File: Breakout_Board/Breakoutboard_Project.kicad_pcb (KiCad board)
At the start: 2 copper layers, 1 part

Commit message: Added costum footprint
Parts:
- added U1: ADXL380-2BCCZ-RL7, ADXL380:CC-14-3_ADI, F.Cu at (97.8, 71.6)
- added U2: STM32F411CCUx, Package_DFN_QFN:QFN-48-1EP_7x7mm_P0.5mm_EP5.6x5.6mm, F.Cu at (100.5, 64.7)

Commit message: added the costum things to main pcb and sch
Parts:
- added U2: ~, SeniorDesignLibrary:BlackpillGeneric, F.Cu at (69.0, 78.1)

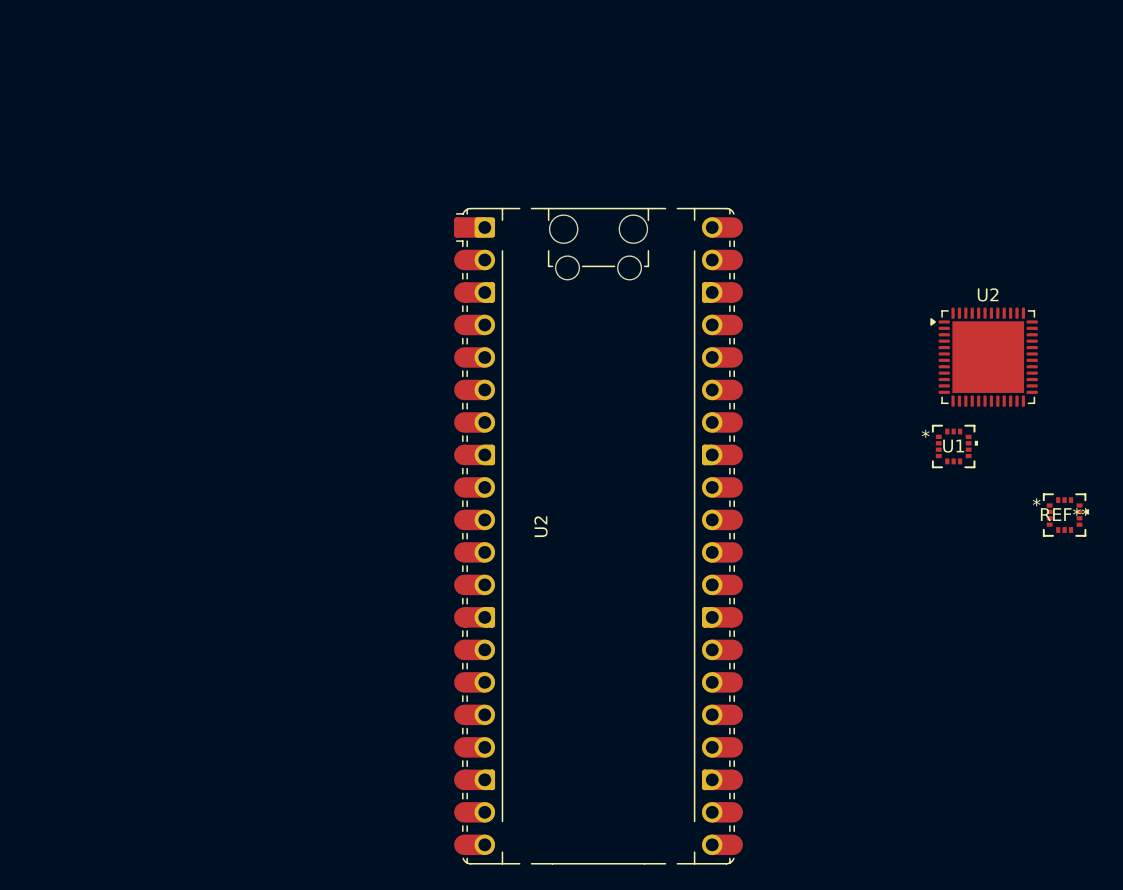
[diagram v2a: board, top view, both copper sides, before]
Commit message: added more organization
heriarchical sheets yay, added all the compoennts we will be working with and seperated into sheets so we can work on the in parralel easier.
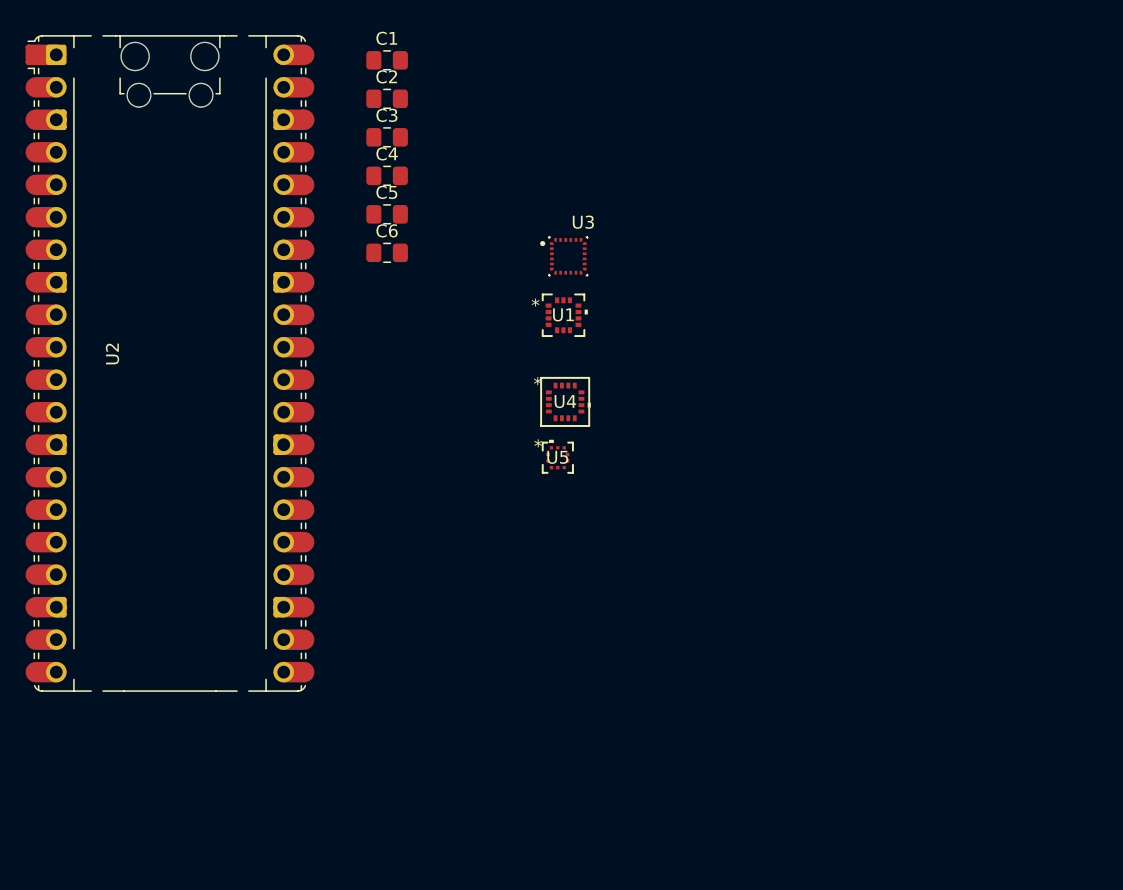
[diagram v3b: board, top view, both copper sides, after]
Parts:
- removed REF**: CC-14-3_ADI, ADXL380:CC-14-3_ADI
- removed the U2 at (69.0, 78.1)
- removed the U2 at (100.5, 64.7)
- added C1: .1uf, Capacitor_SMD:C_0805_2012Metric_Pad1.18x1.45mm_HandSolder, F.Cu at (53.5, 41.5)
- added C2: 1uf, Capacitor_SMD:C_0805_2012Metric_Pad1.18x1.45mm_HandSolder, F.Cu at (53.5, 44.5)
- added C3: 10uf, Capacitor_SMD:C_0805_2012Metric_Pad1.18x1.45mm_HandSolder, F.Cu at (53.5, 47.5)
- added C4: .1uf, Capacitor_SMD:C_0805_2012Metric_Pad1.18x1.45mm_HandSolder, F.Cu at (53.5, 50.5)
- added C5: 1uf, Capacitor_SMD:C_0805_2012Metric_Pad1.18x1.45mm_HandSolder, F.Cu at (53.5, 53.5)
- added C6: 10uf, Capacitor_SMD:C_0805_2012Metric_Pad1.18x1.45mm_HandSolder, F.Cu at (53.5, 56.5)
- added U2: STM32F411, SeniorDesignLibrary:BlackpillGeneric, F.Cu at (35.5, 64.6)
- added U3: ICM-40609-D, ICM-40609-D:XDCR_ICM-40609-D, F.Cu at (67.7, 56.8)
- added U4: MMC5983MA, MMC5983MA:MMC5983MA_MEM, F.Cu at (67.5, 68.2)
- added U5: BMP581, BMP581:QFN10_BMP581_BOS, F.Cu at (66.9, 72.5)
- moved U1 32.2 mm to (67.3, 61.4)

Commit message: changing around some things
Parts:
- added C11: .1uf, Capacitor_SMD:C_0805_2012Metric_Pad1.18x1.45mm_HandSolder, F.Cu at (115.0, 23.5)
- added C12: .1uf, Capacitor_SMD:C_0805_2012Metric_Pad1.18x1.45mm_HandSolder, F.Cu at (115.0, 26.5)
- added C13: .1uf, Capacitor_SMD:C_0805_2012Metric_Pad1.18x1.45mm_HandSolder, F.Cu at (115.0, 29.5)
- added C14: 1uf, Capacitor_SMD:C_0805_2012Metric_Pad1.18x1.45mm_HandSolder, F.Cu at (115.0, 32.5)
- added C15: 1uf, Capacitor_SMD:C_0805_2012Metric_Pad1.18x1.45mm_HandSolder, F.Cu at (115.0, 35.5)
- added C7: .1uf, Capacitor_SMD:C_0805_2012Metric_Pad1.18x1.45mm_HandSolder, F.Cu at (115.0, 14.4)
- added C8: 1uf, Capacitor_SMD:C_0805_2012Metric_Pad1.18x1.45mm_HandSolder, F.Cu at (115.0, 17.4)
- added C9: 10uf, Capacitor_SMD:C_0805_2012Metric_Pad1.18x1.45mm_HandSolder, F.Cu at (115.0, 20.4)
- added D1: ESD5Zxx, Diode_SMD:D_SOD-523, F.Cu at (124.8, 14.2)
- added D2: ESD5Zxx, Diode_SMD:D_SOD-523, F.Cu at (124.8, 16.6)
- added D3: ESD5Zxx, Diode_SMD:D_SOD-523, F.Cu at (119.2, 14.2)
- added D4: ESD5Zxx, Diode_SMD:D_SOD-523, F.Cu at (119.2, 16.6)
- moved U1 66.8 mm to (126.4, 30.2)
- moved U3 66.8 mm to (126.7, 25.6)
- moved U4 66.8 mm to (126.5, 37.0)
- moved U5 66.8 mm to (125.9, 41.4)
- moved C1 61.3 mm to (109.0, 15.4)
- moved C5 61.3 mm to (109.0, 27.5)
- moved C2 61.3 mm to (109.0, 18.5)
- moved C3 61.3 mm to (109.0, 21.5)
- moved C4 61.3 mm to (109.0, 24.5)
- moved C6 61.3 mm to (109.0, 30.5)
- moved U2 5.66 mm to (37.9, 59.5)
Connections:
- U1 pad 1: unconnected-(U1-FSYNC-Pad1) -> /Accel & Gyro/FSYNC_ADXL
- U1 pad 10: unconnected-(U1-VS-Pad10) -> +3.3V
- U1 pad 11: unconnected-(U1-VDDIO-Pad11) -> +3.3V
- U1 pad 2: unconnected-(U1-SCLK/SCL-Pad2) -> /SCLK_Accel_gyro
- U1 pad 3: unconnected-(U1-SDI/SDA-Pad3) -> /MOSI_Accel_gyro
- U1 pad 4: unconnected-(U1-SDO/ASEL0-Pad4) -> /MISO_Accel_gyro
- U1 pad 5: unconnected-(U1-*CS/ASEL1-Pad5) -> /CS_ADXL
- U1 pad 6: unconnected-(U1-INT0-Pad6) -> /Accel & Gyro/INT0_ADXL
- U1 pad 7: unconnected-(U1-INT1-Pad7) -> /Accel & Gyro/INT1_ADXL
- U1 pad 8: unconnected-(U1-V1P8-Pad8) -> Net-(U1-V1P8)
- U1 pad 9: unconnected-(U1-GND-Pad9) -> GND
- U2 pad 29: unconnected-(U2-A3-Pad29) -> /CS_ADXL
- U2 pad 30: unconnected-(U2-A4-Pad30) -> /CS_ICM
- U2 pad 31: unconnected-(U2-A5-Pad31) -> /SCLK_Accel_gyro
- U2 pad 32: unconnected-(U2-A6-Pad32) -> /MISO_Accel_gyro
- U2 pad 33: unconnected-(U2-A7-Pad33) -> /MOSI_Accel_gyro
- U3 pad 11: unconnected-(U3-RESV-Pad11) -> GND
- U3 pad 12: unconnected-(U3-INT1/INT-Pad12) -> /Accel & Gyro/INT1_ICM
- U3 pad 13: unconnected-(U3-VDD-Pad13) -> +3.3V
- U3 pad 18: unconnected-(U3-GND-Pad18) -> GND
- U3 pad 19: unconnected-(U3-INT2/FSYNC-Pad19) -> /Accel & Gyro/FSYNC_ICM
- U3 pad 20: unconnected-(U3-RESV__1-Pad20) -> GND
- U3 pad 22: unconnected-(U3-~{CS}-Pad22) -> /CS_ICM
- U3 pad 23: unconnected-(U3-SCL/SCLK-Pad23) -> /SCLK_Accel_gyro
- U3 pad 24: unconnected-(U3-SDA/SDI/SDIO-Pad24) -> /MOSI_Accel_gyro
- U3 pad 8: unconnected-(U3-VDDIO-Pad8) -> +3.3V
- U3 pad 9: unconnected-(U3-AD0/SDO-Pad9) -> /MISO_Accel_gyro

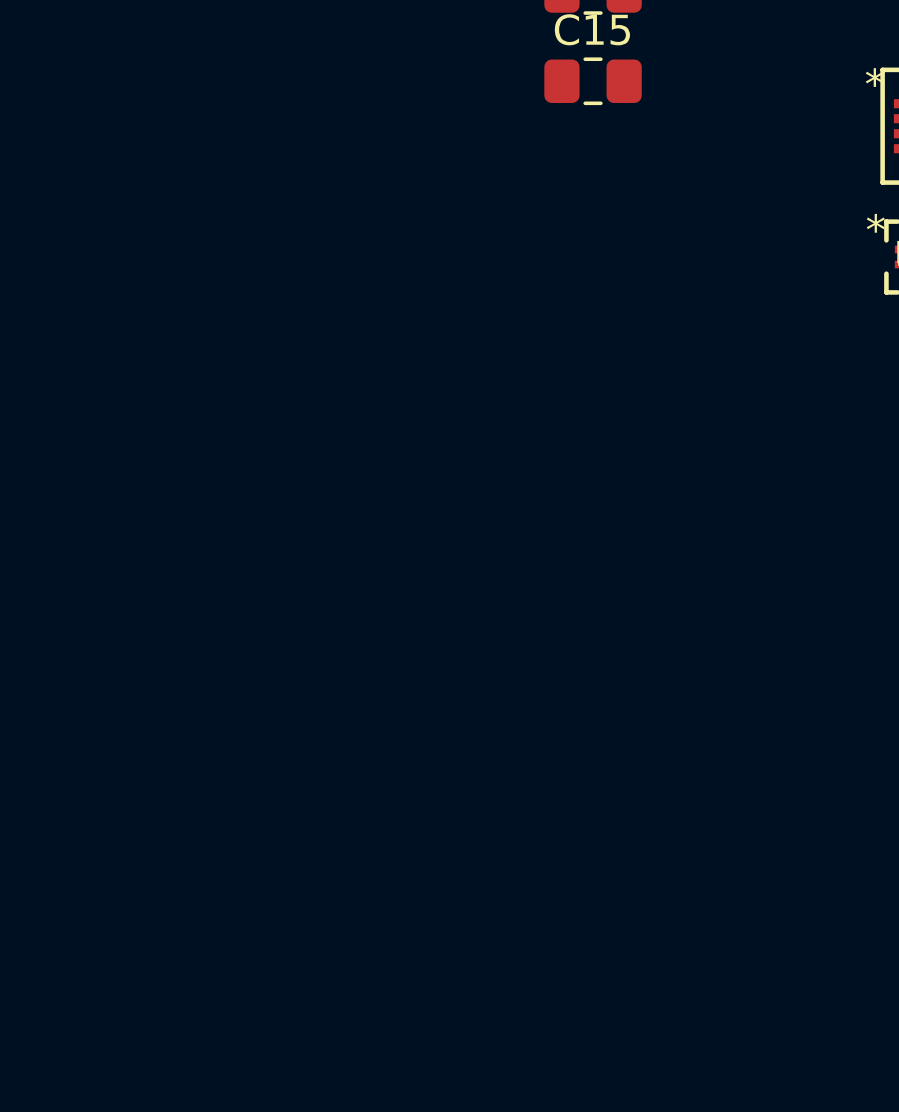
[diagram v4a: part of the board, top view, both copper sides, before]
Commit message: ready for breakout
Fixed up some work, now its ready for breakouts before final PCB layout
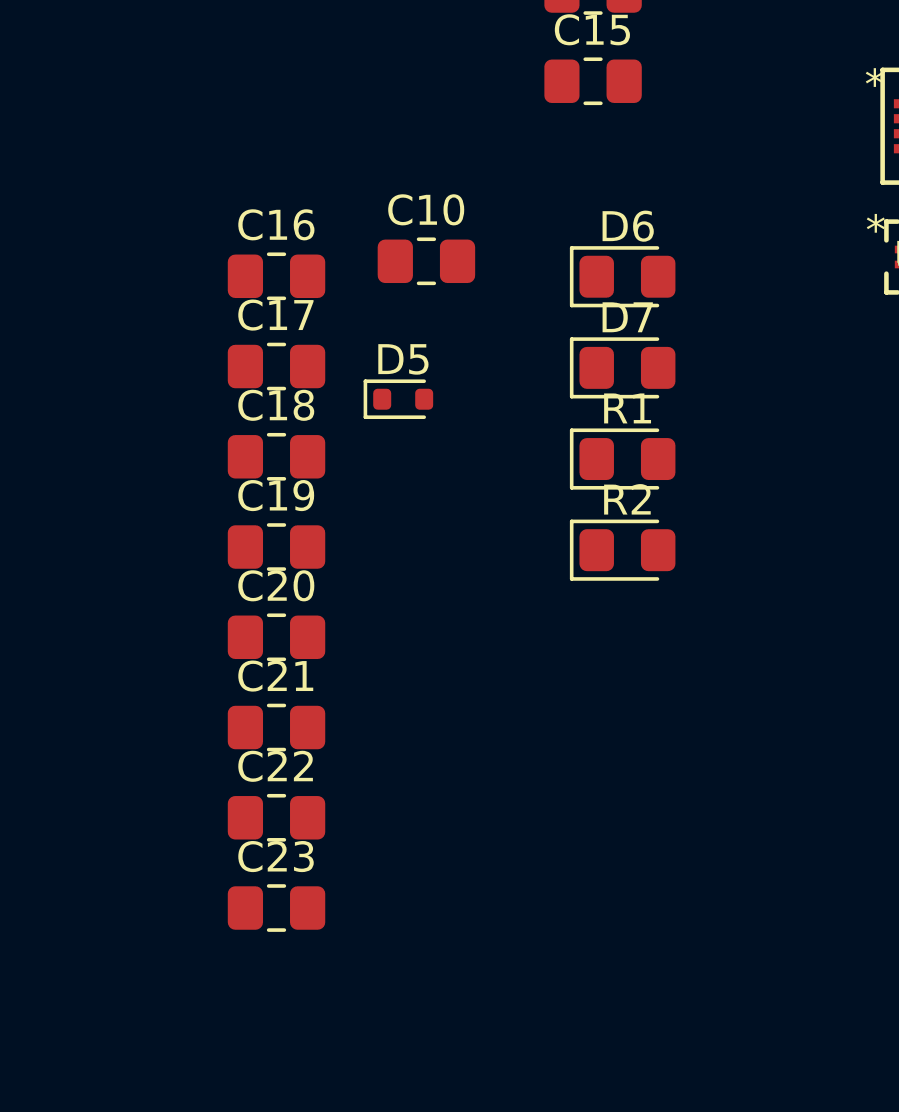
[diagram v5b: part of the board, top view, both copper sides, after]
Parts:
- added C10: 10uf, Capacitor_SMD:C_0805_2012Metric_Pad1.18x1.45mm_HandSolder, F.Cu at (109.4, 41.5)
- added C16: .1uf, Capacitor_SMD:C_0805_2012Metric_Pad1.18x1.45mm_HandSolder, F.Cu at (104.4, 42.0)
- added C17: .1uf, Capacitor_SMD:C_0805_2012Metric_Pad1.18x1.45mm_HandSolder, F.Cu at (104.4, 45.0)
- added C18: 1uf, Capacitor_SMD:C_0805_2012Metric_Pad1.18x1.45mm_HandSolder, F.Cu at (104.4, 48.0)
- added C19: 1uf, Capacitor_SMD:C_0805_2012Metric_Pad1.18x1.45mm_HandSolder, F.Cu at (104.4, 51.0)
- added C20: .1uf, Capacitor_SMD:C_0805_2012Metric_Pad1.18x1.45mm_HandSolder, F.Cu at (104.4, 54.0)
- added C21: .1uf, Capacitor_SMD:C_0805_2012Metric_Pad1.18x1.45mm_HandSolder, F.Cu at (104.4, 57.1)
- added C22: 1uf, Capacitor_SMD:C_0805_2012Metric_Pad1.18x1.45mm_HandSolder, F.Cu at (104.4, 60.1)
- added C23: 1uf, Capacitor_SMD:C_0805_2012Metric_Pad1.18x1.45mm_HandSolder, F.Cu at (104.4, 63.1)
- added D5: ESD5Zxx, Diode_SMD:D_SOD-523, F.Cu at (108.6, 46.1)
- added D6: LED, LED_SMD:LED_0805_2012Metric_Pad1.15x1.40mm_HandSolder, F.Cu at (116.1, 42.0)
- added D7: LED, LED_SMD:LED_0805_2012Metric_Pad1.15x1.40mm_HandSolder, F.Cu at (116.1, 45.1)
- added R1: R, LED_SMD:LED_0805_2012Metric_Pad1.15x1.40mm_HandSolder, F.Cu at (116.1, 48.1)
- added R2: R, LED_SMD:LED_0805_2012Metric_Pad1.15x1.40mm_HandSolder, F.Cu at (116.1, 51.1)
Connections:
- U1 pad 1: /Accel & Gyro/FSYNC_ADXL -> /FSYNC_ADXL
- U1 pad 2: /SCLK_Accel_gyro -> /SCLK
- U1 pad 3: /MOSI_Accel_gyro -> /MOSI
- U1 pad 4: /MISO_Accel_gyro -> /MISO
- U1 pad 6: /Accel & Gyro/INT0_ADXL -> /ADXL_INT0
- U1 pad 7: /Accel & Gyro/INT1_ADXL -> /ADXL_INT1
- U2 pad 10: unconnected-(U2-A15-Pad10) -> /ICM_INT1
- U2 pad 11: unconnected-(U2-B3-Pad11) -> /FSYNC_ADXL
- U2 pad 12: unconnected-(U2-B4-Pad12) -> /FSYNC_ICM
- U2 pad 2: unconnected-(U2-B13-Pad2) -> /Baro_INT
- U2 pad 27: unconnected-(U2-A1-Pad27) -> /CS_MAG
- U2 pad 28: unconnected-(U2-A2-Pad28) -> /CS_BARO
- U2 pad 3: unconnected-(U2-B14-Pad3) -> /Mag_INT
- U2 pad 31: /SCLK_Accel_gyro -> /SCLK
- U2 pad 32: /MISO_Accel_gyro -> /MISO
- U2 pad 33: /MOSI_Accel_gyro -> /MOSI
- U2 pad 8: unconnected-(U2-A11-Pad8) -> /ADXL_INT0
- U2 pad 9: unconnected-(U2-A12-Pad9) -> /ADXL_INT1
- U3 pad 12: /Accel & Gyro/INT1_ICM -> /ICM_INT1
- U3 pad 19: /Accel & Gyro/FSYNC_ICM -> /FSYNC_ICM
- U3 pad 23: /SCLK_Accel_gyro -> /SCLK
- U3 pad 24: /MOSI_Accel_gyro -> /MOSI
- U3 pad 9: /MISO_Accel_gyro -> /MISO
- U4 pad 1: unconnected-(U4-SCL/SPI_SCK-Pad1) -> /SCLK
- U4 pad 10: unconnected-(U4-CAP-Pad10) -> Net-(U4-CAP)
- U4 pad 11: unconnected-(U4-GND-Pad11) -> GND
- U4 pad 13: unconnected-(U4-VDDIO-Pad13) -> +3.3V
- U4 pad 15: unconnected-(U4-INT-Pad15) -> /Mag_INT
- U4 pad 16: unconnected-(U4-SDA/SPI_SDI-Pad16) -> /MOSI
- U4 pad 2: unconnected-(U4-VDD-Pad2) -> +3.3V
- U4 pad 4: unconnected-(U4-SPI_CS-Pad4) -> /CS_MAG
- U4 pad 5: unconnected-(U4-SPI_SDO-Pad5) -> /MISO
- U4 pad 9: unconnected-(U4-GND-Pad9) -> GND
- U5 pad 1: unconnected-(U5-VDDIO-Pad1) -> +3.3V
- U5 pad 10: unconnected-(U5-VDD-Pad10) -> +3.3V
- U5 pad 2: unconnected-(U5-SCK-Pad2) -> /SCLK
- U5 pad 3: unconnected-(U5-VSS-Pad3) -> GND
- U5 pad 4: unconnected-(U5-SDI-Pad4) -> /MOSI
- U5 pad 5: unconnected-(U5-SDO-Pad5) -> /MISO
- U5 pad 6: unconnected-(U5-CSB-Pad6) -> /CS_BARO
- U5 pad 7: unconnected-(U5-INT-Pad7) -> /Baro_INT
- U5 pad 8: unconnected-(U5-VSS-Pad8) -> GND
- U5 pad 9: unconnected-(U5-VSS-Pad9) -> GND

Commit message: some layout
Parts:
- added J1: Conn_01x17, Connector_PinHeader_2.54mm:PinHeader_1x17_P2.54mm_Vertical, F.Cu at (28.0, 36.9)
- added J2: Conn_01x17, Connector_PinHeader_2.54mm:PinHeader_1x17_P2.54mm_Vertical, F.Cu at (57.0, 85.2)
- added J3: Conn_02x06_Top_Bottom, Connector_PinHeader_1.27mm:PinHeader_2x06_P1.27mm_Vertical, F.Cu at (72.7, 73.7)
- added J4: Conn_01x04, Connector_PinSocket_2.54mm:PinSocket_1x04_P2.54mm_Vertical, F.Cu at (72.5, 41.2)
- moved U1 82.4 mm to (64.5, 84.7)
- moved U3 76.0 mm to (64.0, 68.5)
- moved U5 62.8 mm to (64.0, 52.2)
- moved U4 62.8 mm to (63.8, 35.8)
- moved C1 46.1 mm to (155.1, 16.4)
- moved C10 46.1 mm to (155.5, 42.4)
- moved C11 46.1 mm to (161.0, 24.4)
- moved C12 46.1 mm to (161.0, 27.4)
- moved C13 46.1 mm to (161.0, 30.4)
- moved C14 46.1 mm to (161.0, 33.4)
- moved C15 46.1 mm to (161.0, 36.4)
- moved C16 46.1 mm to (150.5, 42.9)
- moved C17 46.1 mm to (150.5, 46.0)
- moved C18 46.1 mm to (150.5, 49.0)
- moved C19 46.1 mm to (150.5, 52.0)
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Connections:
- U2 pad 1: unconnected-(U2-B12-Pad1) -> /B12
- U2 pad 13: unconnected-(U2-B5-Pad13) -> /B5
- U2 pad 14: unconnected-(U2-15-Pad14) -> /B6
- U2 pad 15: unconnected-(U2-B7-Pad15) -> /B7
- U2 pad 16: unconnected-(U2-B8-Pad16) -> /B8
- U2 pad 17: unconnected-(U2-B9-Pad17) -> /B9
- U2 pad 21: unconnected-(U2-VB-Pad21) -> /VB
- U2 pad 22: unconnected-(U2-C13-Pad22) -> /C13
- U2 pad 23: unconnected-(U2-C14-Pad23) -> /C14
- U2 pad 24: unconnected-(U2-C15-Pad24) -> /C15
- U2 pad 25: unconnected-(U2-R-Pad25) -> /R
- U2 pad 26: unconnected-(U2-A0-Pad26) -> /A0
- U2 pad 34: unconnected-(U2-B0-Pad34) -> /B0
- U2 pad 35: unconnected-(U2-B1-Pad35) -> /B1
- U2 pad 36: unconnected-(U2-B2-Pad36) -> /B2
- U2 pad 37: unconnected-(U2-B10-Pad37) -> /B10
- U2 pad 4: unconnected-(U2-B15-Pad4) -> /B15
- U2 pad 5: unconnected-(U2-A8-Pad5) -> /A8
- U2 pad 6: unconnected-(U2-A9-Pad6) -> /A9
- U2 pad 7: unconnected-(U2-A10-Pad7) -> /A10
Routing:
- net GND: track 0.00 -> 5.46 mm, vias 0 -> 2
- net +3.3V: track 0.00 -> 2.62 mm
- added copper zone on F.Cu, net +3.3V
- added copper zone on B.Cu, net GND
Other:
- board outline added: 55.5 x 56.5 mm

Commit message: helo
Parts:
- moved C1 73.9 mm to (83.1, 33.4)
- moved C10 73.9 mm to (83.5, 59.4)
- moved C11 73.9 mm to (89.1, 41.4)
- moved C12 73.9 mm to (89.1, 44.4)
- moved C13 73.9 mm to (89.1, 47.4)
- moved C14 73.9 mm to (89.1, 50.4)
- moved C15 73.9 mm to (89.1, 53.4)
- moved C16 73.9 mm to (78.5, 59.9)
- moved C17 73.9 mm to (78.5, 62.9)
- moved C18 73.9 mm to (78.5, 66.0)
- moved C19 73.9 mm to (78.5, 69.0)
- moved C2 73.9 mm to (83.1, 36.4)
- moved C20 73.9 mm to (78.5, 72.0)
- moved C21 73.9 mm to (78.5, 75.0)
- moved C22 73.9 mm to (78.5, 78.0)
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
